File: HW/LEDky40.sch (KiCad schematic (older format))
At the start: 0 parts

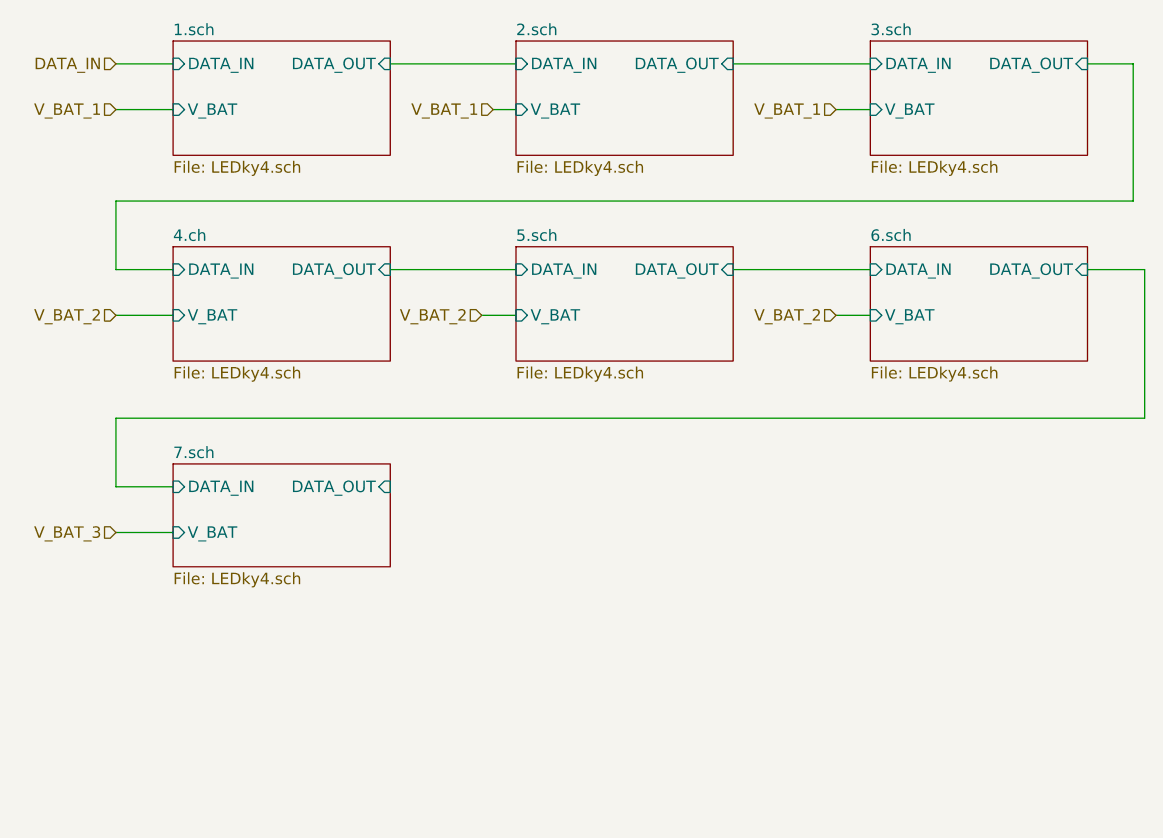
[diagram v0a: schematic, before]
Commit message: change structure of LEDs, add switching power supply of LEDs in parts
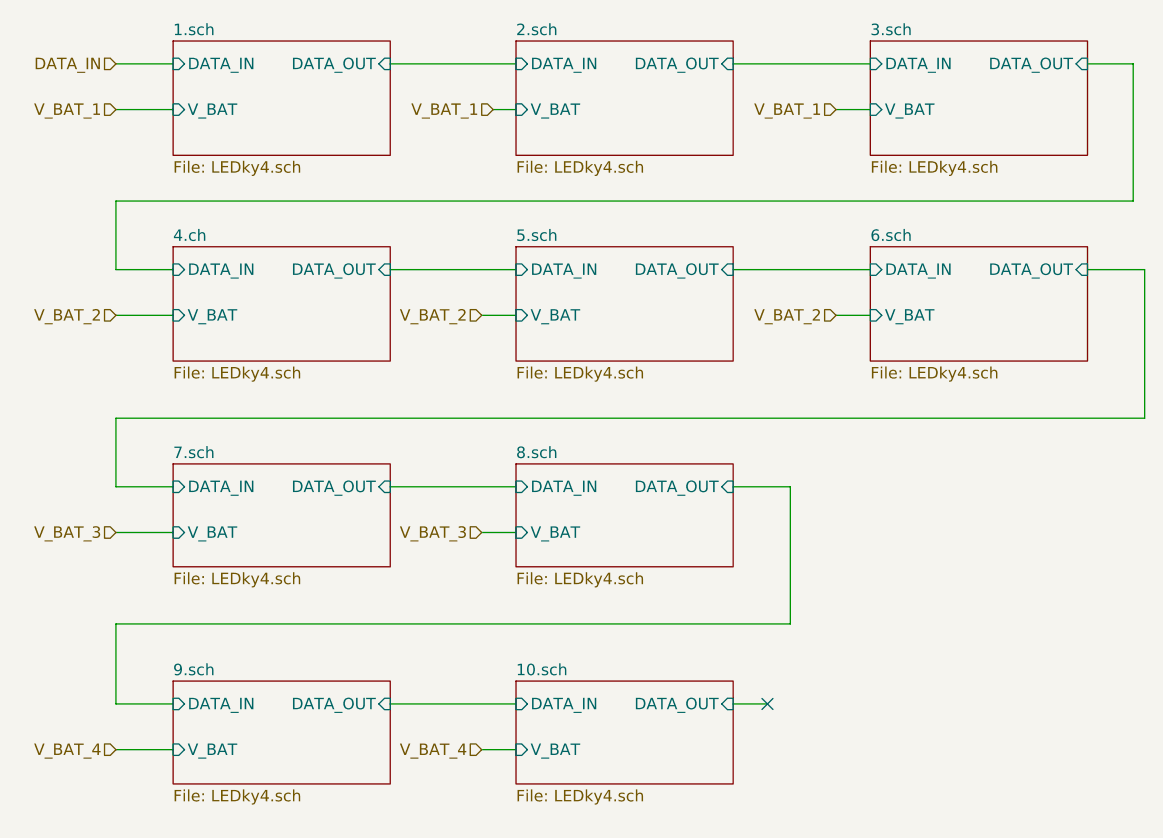
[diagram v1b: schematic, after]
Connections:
- no-connect marks 0 -> 1
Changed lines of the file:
@@
 $Descr A4 11693 8268
 encoding utf-8
-Sheet 3 28
+Sheet 3 42
 Title ""
 Date ""
@@
 Wire Wire Line
 	1250 2850 1000 2850
+$Sheet
+S 2750 2550 950  450
+U 5F79845A
+F0 "8.sch" 50
+F1 "LEDky4.sch" 50
+F2 "DATA_IN" I L 2750 2650 50
+F3 "DATA_OUT" I R 3700 2650 50
+F4 "V_BAT" I L 2750 2850 50
+$EndSheet
+$Sheet
+S 1250 3500 950  450
+U 5F79846B
+F0 "9.sch" 50
+F1 "LEDky4.sch" 50
+F2 "DATA_IN" I L 1250 3600 50
+F3 "DATA_OUT" I R 2200 3600 50
+F4 "V_BAT" I L 1250 3800 50
+$EndSheet
+$Sheet
+S 2750 3500 950  450
+U 5F798482
+F0 "10.sch" 50
+F1 "LEDky4.sch" 50
+F2 "DATA_IN" I L 2750 3600 50
+F3 "DATA_OUT" I R 3700 3600 50
+F4 "V_BAT" I L 2750 3800 50
+$EndSheet
+Text HLabel 1000 3800 0    50   Input ~ 0
+V_BAT_4
+Wire Wire Line
+	2200 2650 2750 2650
+Wire Wire Line
+	3700 2650 3950 2650
+Wire Wire Line
+	3950 2650 3950 3250
+Wire Wire Line
+	3950 3250 1000 3250
+Wire Wire Line
+	1000 3250 1000 3600
+Wire Wire Line
+	1000 3600 1250 3600
+Wire Wire Line
+	1250 3800 1000 3800
+Wire Wire Line
+	2200 3600 2750 3600
+Text HLabel 2600 3800 0    50   Input ~ 0
+V_BAT_4
+Wire Wire Line
+	2600 3800 2750 3800
+Text HLabel 2600 2850 0    50   Input ~ 0
+V_BAT_3
+Wire Wire Line
+	2600 2850 2750 2850
+Wire Wire Line
+	3700 3600 3850 3600
+NoConn ~ 3850 3600
 $EndSCHEMATC

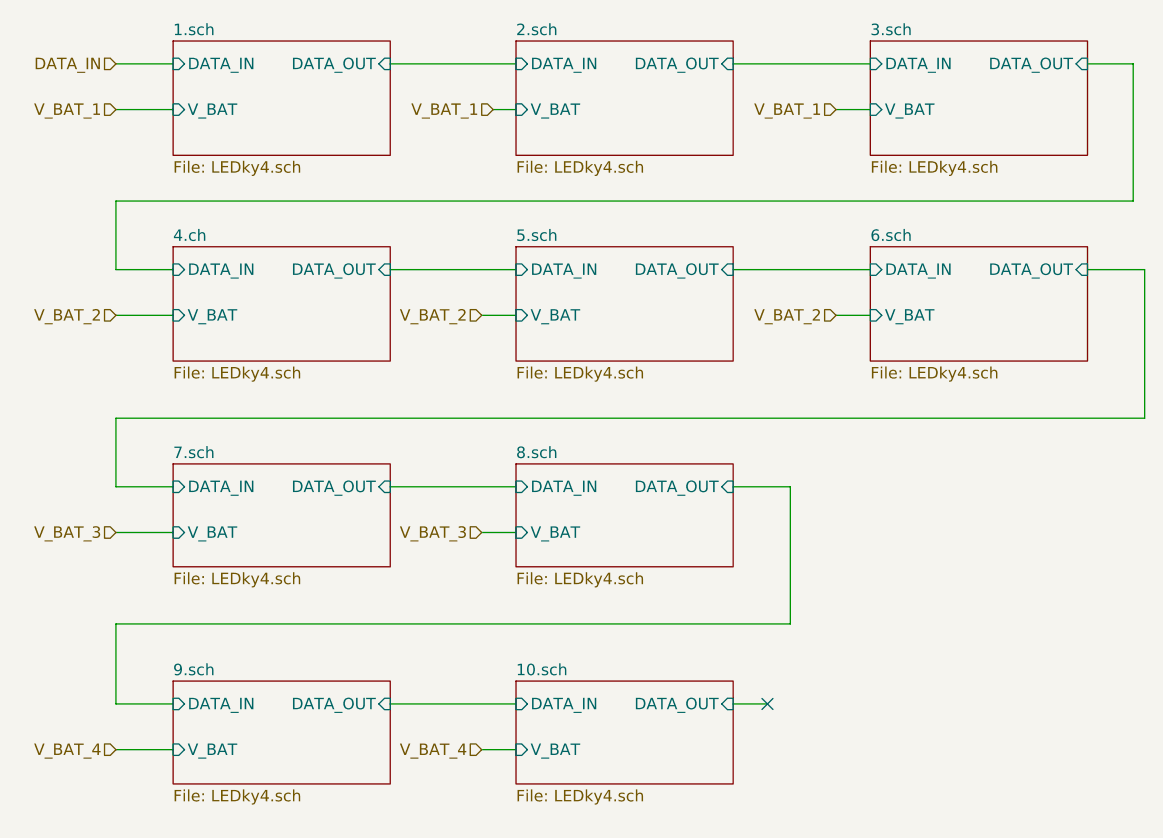
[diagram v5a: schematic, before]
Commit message: make smaller test version, start routing
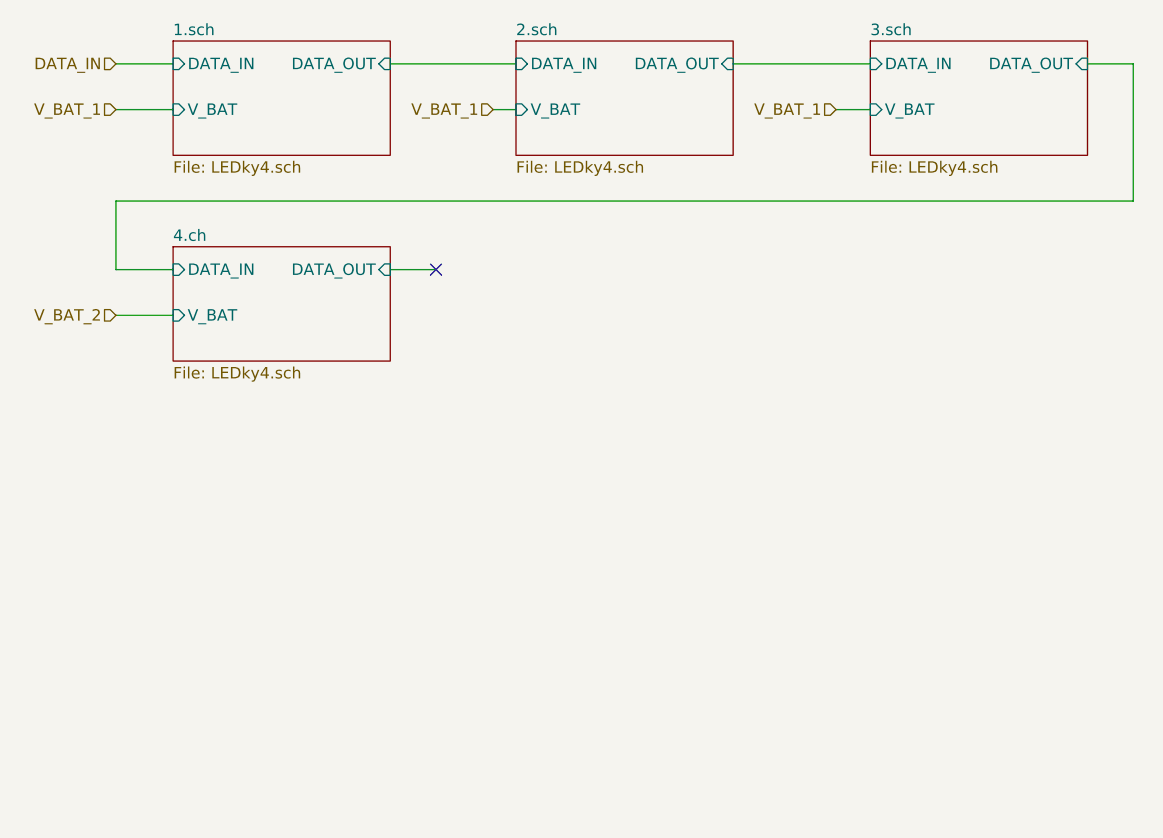
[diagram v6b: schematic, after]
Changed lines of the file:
@@
 $Descr A4 11693 8268
 encoding utf-8
-Sheet 21 44
+Sheet 26 34
 Title ""
 Date ""
@@
 Wire Wire Line
 	1250 1900 1000 1900
-$Sheet
-S 2750 1600 950  500
-U 5F79516D
-F0 "5.sch" 50
-F1 "LEDky4.sch" 50
-F2 "DATA_IN" I L 2750 1700 50
-F3 "DATA_OUT" I R 3700 1700 50
-F4 "V_BAT" I L 2750 1900 50
-$EndSheet
-Text HLabel 2600 1900 0    50   Input ~ 0
-V_BAT_2
 Wire Wire Line
-	2750 1700 2200 1700
-Wire Wire Line
-	2750 1900 2600 1900
-$Sheet
-S 4300 1600 950  500
-U 5F795CD3
-F0 "6.sch" 50
-F1 "LEDky4.sch" 50
-F2 "DATA_IN" I L 4300 1700 50
-F3 "DATA_OUT" I R 5250 1700 50
-F4 "V_BAT" I L 4300 1900 50
-$EndSheet
-Wire Wire Line
-	3700 1700 4300 1700
-Text HLabel 4150 1900 0    50   Input ~ 0
-V_BAT_2
-Wire Wire Line
-	4150 1900 4300 1900
-$Sheet
-S 1250 2550 950  450
-U 5F79747A
-F0 "7.sch" 50
-F1 "LEDky4.sch" 50
-F2 "DATA_IN" I L 1250 2650 50
-F3 "DATA_OUT" I R 2200 2650 50
-F4 "V_BAT" I L 1250 2850 50
-$EndSheet
-Text HLabel 1000 2850 0    50   Input ~ 0
-V_BAT_3
-Wire Wire Line
-	1250 2650 1000 2650
-Wire Wire Line
-	1000 2650 1000 2350
-Wire Wire Line
-	1000 2350 5500 2350
-Wire Wire Line
-	5500 2350 5500 1700
-Wire Wire Line
-	5500 1700 5250 1700
-Wire Wire Line
-	1250 2850 1000 2850
-$Sheet
-S 2750 2550 950  450
-U 5F79845A
-F0 "8.sch" 50
-F1 "LEDky4.sch" 50
-F2 "DATA_IN" I L 2750 2650 50
-F3 "DATA_OUT" I R 3700 2650 50
-F4 "V_BAT" I L 2750 2850 50
-$EndSheet
-$Sheet
-S 1250 3500 950  450
-U 5F79846B
-F0 "9.sch" 50
-F1 "LEDky4.sch" 50
-F2 "DATA_IN" I L 1250 3600 50
-F3 "DATA_OUT" I R 2200 3600 50
-F4 "V_BAT" I L 1250 3800 50
-$EndSheet
-$Sheet
-S 2750 3500 950  450
-U 5F798482
-F0 "10.sch" 50
-F1 "LEDky4.sch" 50
-F2 "DATA_IN" I L 2750 3600 50
-F3 "DATA_OUT" I R 3700 3600 50
-F4 "V_BAT" I L 2750 3800 50
-$EndSheet
-Text HLabel 1000 3800 0    50   Input ~ 0
-V_BAT_4
-Wire Wire Line
-	2200 2650 2750 2650
-Wire Wire Line
-	3700 2650 3950 2650
-Wire Wire Line
-	3950 2650 3950 3250
-Wire Wire Line
-	3950 3250 1000 3250
-Wire Wire Line
-	1000 3250 1000 3600
-Wire Wire Line
-	1000 3600 1250 3600
-Wire Wire Line
-	1250 3800 1000 3800
-Wire Wire Line
-	2200 3600 2750 3600
-Text HLabel 2600 3800 0    50   Input ~ 0
-V_BAT_4
-Wire Wire Line
-	2600 3800 2750 3800
-Text HLabel 2600 2850 0    50   Input ~ 0
-V_BAT_3
-Wire Wire Line
-	2600 2850 2750 2850
-Wire Wire Line
-	3700 3600 3850 3600
-NoConn ~ 3850 3600
+	2200 1700 2400 1700
+NoConn ~ 2400 1700
 $EndSCHEMATC

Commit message: deposit of DPS, start v1.0
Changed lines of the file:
@@
 $Descr A4 11693 8268
 encoding utf-8
-Sheet 26 21
+Sheet 18 30
 Title ""
 Date ""
@@
 Wire Wire Line
 	1250 1900 1000 1900
+$Sheet
+S 2750 1600 950  500
+U 5FB7721A
+F0 "5.sch" 50
+F1 "LEDky4.sch" 50
+F2 "DATA_IN" I L 2750 1700 50
+F3 "DATA_OUT" I R 3700 1700 50
+F4 "V_BAT" I L 2750 1900 50
+$EndSheet
+$Sheet
+S 4300 1600 950  500
+U 5FB77C34
+F0 "6.sch" 50
+F1 "LEDky4.sch" 50
+F2 "DATA_IN" I L 4300 1700 50
+F3 "DATA_OUT" I R 5250 1700 50
+F4 "V_BAT" I L 4300 1900 50
+$EndSheet
+$Sheet
+S 1250 2500 950  500
+U 5FB77C64
+F0 "7.sch" 50
+F1 "LEDky4.sch" 50
+F2 "DATA_IN" I L 1250 2600 50
+F3 "DATA_OUT" I R 2200 2600 50
+F4 "V_BAT" I L 1250 2800 50
+$EndSheet
+$Sheet
+S 2750 2500 950  500
+U 5FB77C81
+F0 "8.sch" 50
+F1 "LEDky4.sch" 50
+F2 "DATA_IN" I L 2750 2600 50
+F3 "DATA_OUT" I R 3700 2600 50
+F4 "V_BAT" I L 2750 2800 50
+$EndSheet
+$Sheet
+S 4300 2500 950  500
+U 5FB77C9B
+F0 "9.sch" 50
+F1 "LEDky4.sch" 50
+F2 "DATA_IN" I L 4300 2600 50
+F3 "DATA_OUT" I R 5250 2600 50
+F4 "V_BAT" I L 4300 2800 50
+$EndSheet
+$Sheet
+S 1250 3500 950  500
+U 5FB77CB0
+F0 "10.sch" 50
+F1 "LEDky4.sch" 50
+F2 "DATA_IN" I L 1250 3600 50
+F3 "DATA_OUT" I R 2200 3600 50
+F4 "V_BAT" I L 1250 3800 50
+$EndSheet
 Wire Wire Line
-	2200 1700 2400 1700
-NoConn ~ 2400 1700
+	2200 1700 2750 1700
+Wire Wire Line
+	3700 1700 4300 1700
+Wire Wire Line
+	5250 1700 5450 1700
+Wire Wire Line
+	5450 1700 5450 2300
+Wire Wire Line
+	5450 2300 1000 2300
+Wire Wire Line
+	1000 2300 1000 2600
+Wire Wire Line
+	1000 2600 1250 2600
+Wire Wire Line
+	2200 2600 2750 2600
+Wire Wire Line
+	3700 2600 4300 2600
+Wire Wire Line
+	5250 2600 5450 2600
+Wire Wire Line
+	5450 2600 5450 3150
+Wire Wire Line
+	5450 3150 1000 3150
+Wire Wire Line
+	1000 3150 1000 3600
+Wire Wire Line
+	1000 3600 1250 3600
+Wire Wire Line
+	2200 3600 2350 3600
+NoConn ~ 2350 3600
+Text HLabel 2650 1900 0    50   Input ~ 0
+V_BAT_2
+Text HLabel 4150 1900 0    50   Input ~ 0
+V_BAT_2
+Wire Wire Line
+	4300 1900 4150 1900
+Wire Wire Line
+	2750 1900 2650 1900
+Text HLabel 1000 2800 0    50   Input ~ 0
+V_BAT_3
+Text HLabel 2650 2800 0    50   Input ~ 0
+V_BAT_3
+Wire Wire Line
+	2750 2800 2650 2800
+Wire Wire Line
+	1250 2800 1000 2800
+Text HLabel 4150 2800 0    50   Input ~ 0
+V_BAT_4
+Text HLabel 1000 3800 0    50   Input ~ 0
+V_BAT_4
+Wire Wire Line
+	4300 2800 4150 2800
+Wire Wire Line
+	1250 3800 1000 3800
 $EndSCHEMATC
